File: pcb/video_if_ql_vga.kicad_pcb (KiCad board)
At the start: 2 copper layers, 31.1 x 66.2 mm, 16 parts, among them J1 Conn_01x05, J2 DB15_Female_HighDensity, U1 SC0915

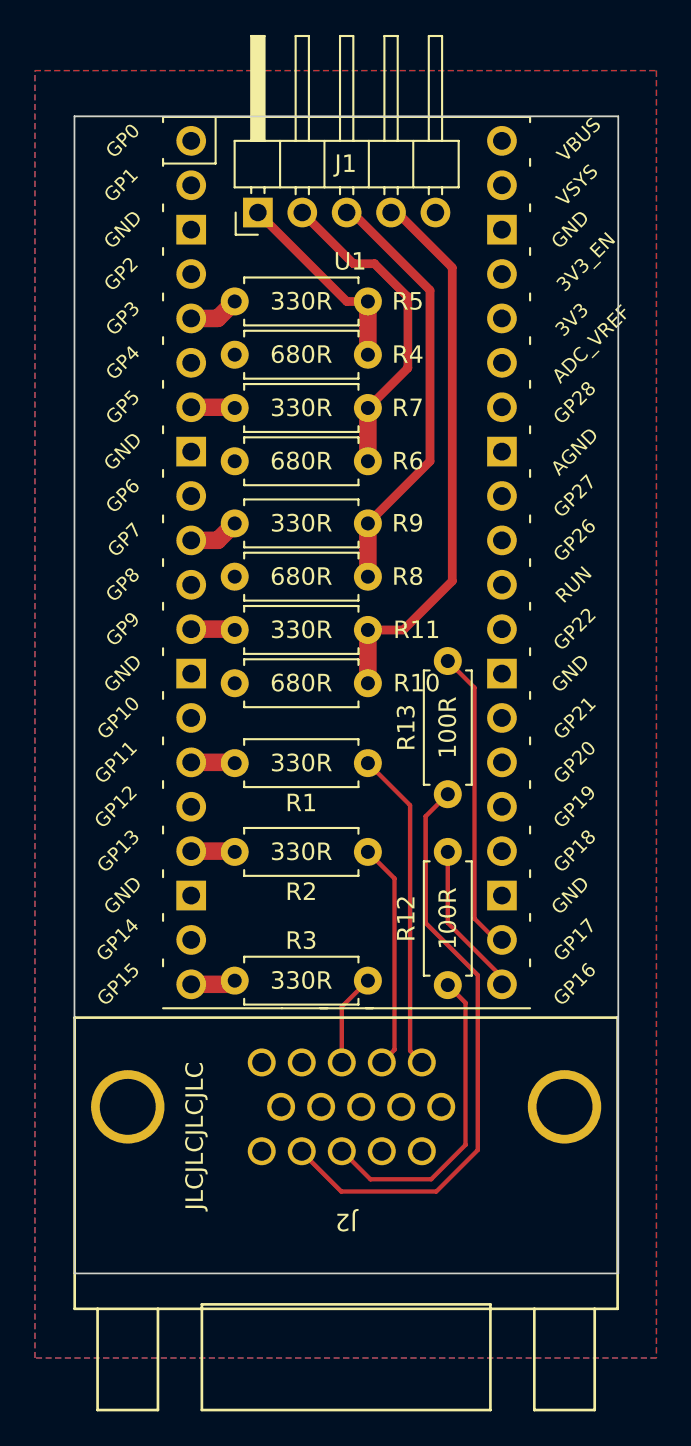
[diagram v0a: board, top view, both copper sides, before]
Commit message: Fix mistake in voltage divider
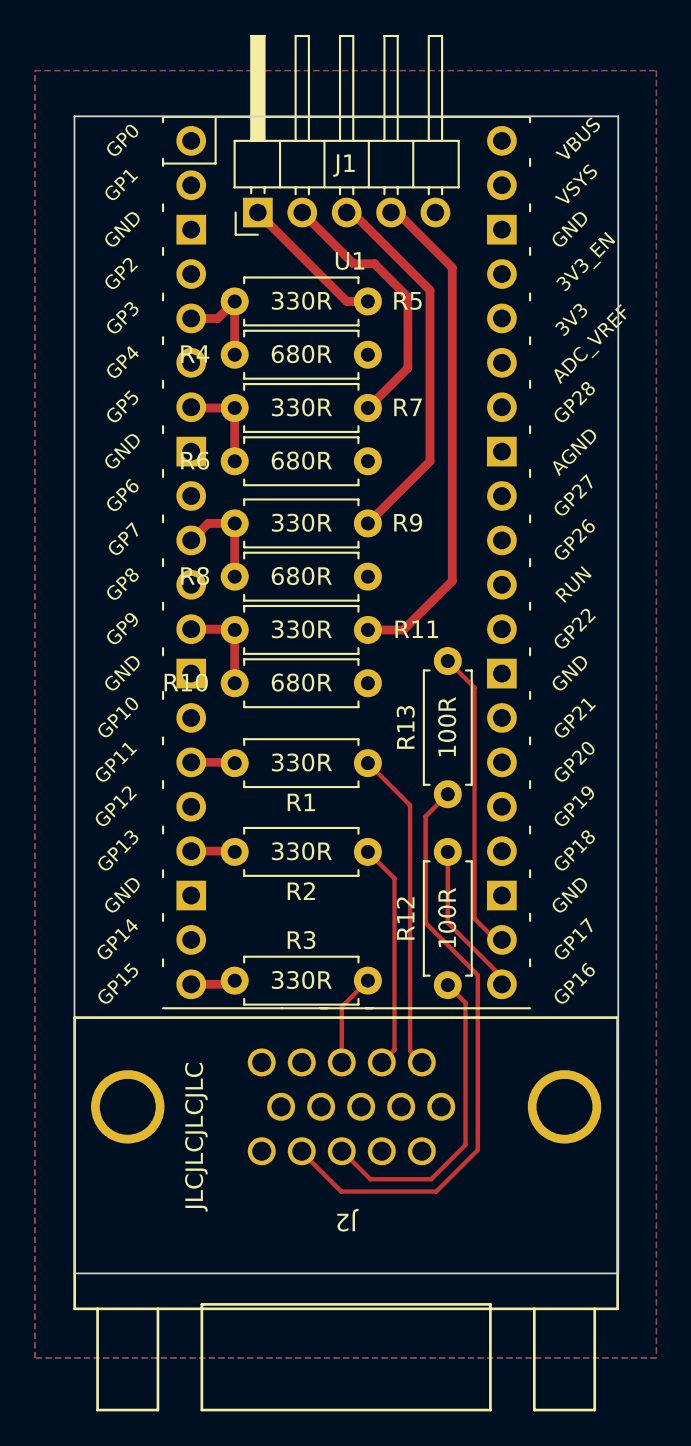
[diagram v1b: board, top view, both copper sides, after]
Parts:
- moved R10 7.62 mm to (135.9, 90.9), turned to 0 degrees
- moved R4 7.62 mm to (143.5, 72.1), turned to 180 degrees
- moved R6 7.62 mm to (135.9, 78.2), turned to 0 degrees
- moved R8 7.62 mm to (143.5, 84.8), turned to 180 degrees
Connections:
- R10 pad 1: Net-(J1-Pad4) -> /QLSYNC
- R4 pad 2: Net-(J1-Pad1) -> /QLRED
- R6 pad 1: Net-(J1-Pad2) -> /QLGREEN
- R8 pad 2: Net-(J1-Pad3) -> /QLBLUE
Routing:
- net /QLGREEN: track 2.51 -> 5.62 mm
- net Net-(J1-Pad2): track 18.4 -> 15.3 mm
- net /QLSYNC: track 2.51 -> 5.56 mm
- net Net-(J1-Pad4): track 31.8 -> 28.7 mm
- net Net-(J1-Pad3): track 24.5 -> 21.4 mm
- net Net-(J1-Pad1): track 11.5 -> 8.40 mm
- net /QLRED: track 2.89 -> 5.94 mm
- net /QLBLUE: track 2.89 -> 5.94 mm

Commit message: Add smd footprints for resistors
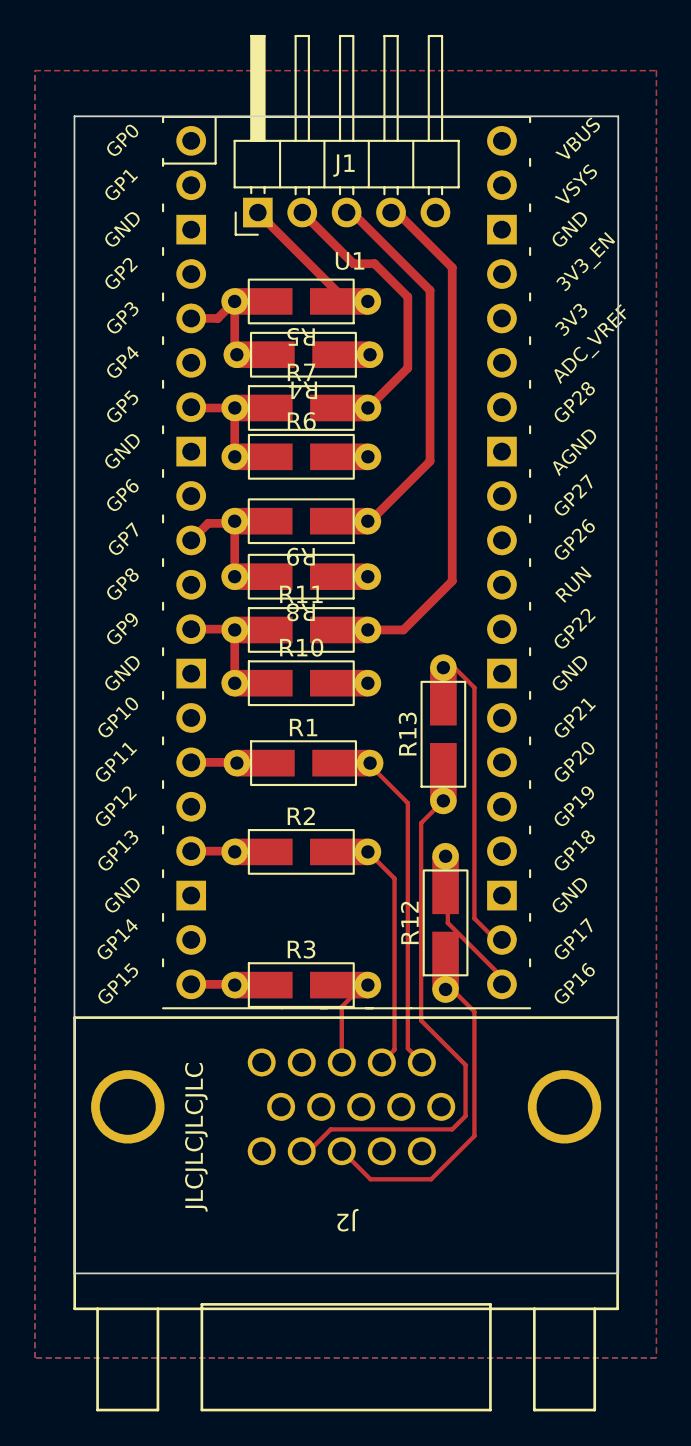
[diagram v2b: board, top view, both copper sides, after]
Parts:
- R1, R10, R11, R12, R13, R2, R3, R4, R5, R6, R7, R8, R9: footprint Resistor_THT:R_Axial_DIN0207_L6.3mm_D2.5mm_P7.62mm_Horizontal -> THT_SMD:R_Axial_DIN0207_L6.3mm_D2.5mm_P7.62_Horizontal
- moved R1 3.94 mm to (139.8, 95.5)
- moved R6 3.82 mm to (139.7, 78.0)
- moved R3 3.82 mm to (139.7, 108.2)
- moved R9 3.82 mm to (139.7, 81.7)
- moved R7 3.81 mm to (139.7, 75.2)
- moved R5 3.81 mm to (139.7, 69.1)
- moved R8 3.81 mm to (139.7, 84.8)
- moved R10 3.81 mm to (139.7, 90.9)
- moved R11 3.81 mm to (139.7, 87.9)
- moved R2 3.81 mm to (139.7, 100.6)
- moved R4 3.69 mm to (139.8, 72.1)
- moved R12 3.56 mm to (148.0, 104.6)
- moved R13 3.44 mm to (147.8, 93.9)
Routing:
- net Net-(J2-Pad14): track 34.2 -> 29.9 mm
